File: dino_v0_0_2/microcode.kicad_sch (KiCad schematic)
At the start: 10 parts, among them U15 AT28C64B, U16 74LS244N, U17 74LS244N, U23 AT28C64B, U9 AT28C64B

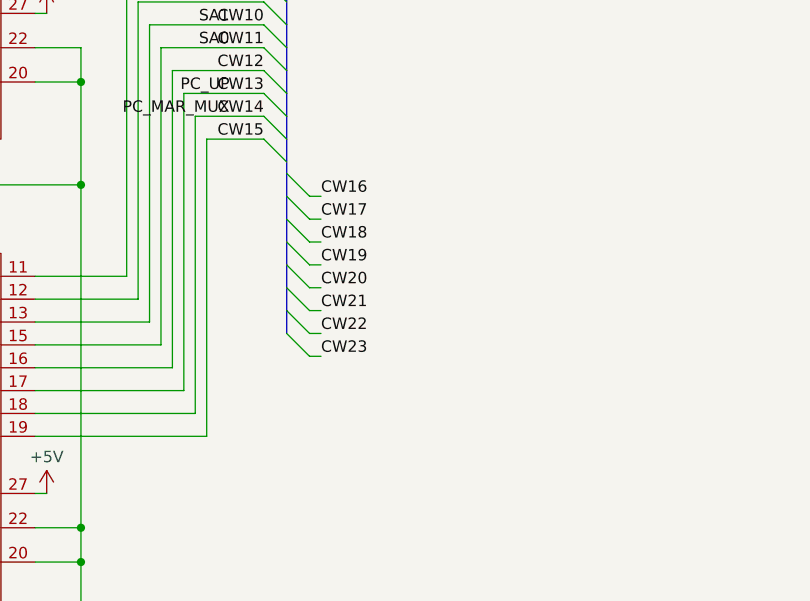
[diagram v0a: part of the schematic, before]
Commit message: feat: Phase F/F+ ISA: 174 instructions, timing fixes, and robust tooling
This commit integrates Phase F and F+ of the ISA, expanding the instruction set to 174 instructions. This includes:
- New conditional branch `JNC`, register-to-register moves, SP/PC readbacks and manipulation (HLSP/SPHL, INXSP/DCXSP).
- Indexed memory access (LDAX/STAX), SP-relative memory access (LDAS/STAS), and memory-indirect addressing (LDAM/STAM/JMPM, etc.) as a new addressing mode.
- Immediate ALU operations (ADI, SUI, ANI, etc.) and ALU results directly to B/C or memory.
- Compare-only instructions (CMP, TST).
- The `IN` opcode has been fully retired from the ISA as of 2026-08-27, and `0x00` confirmed as `NOP`.

Crucially, this commit resolves several critical hardware stability issues:
- Eliminated random machine halts by replacing a damaged `74HC14` (`U56`) and rewiring the reset chain.
- Fixed intermittent failures in `PROG_isasoak` due to ground bounce by starring GND/VCC connections (2026-09-01).
- Introduced microcode-level "SETTLE" states for 23 ALU instructions to ensure timing margins at 1.024MHz, resolving timing-dependent failures for instructions that load and consume operands in consecutive T-states.

The development tooling has also been significantly improved for robustness and accuracy:
- The assembler (`asm.py`) now uses `microcode_gen.py` as the single source of truth for ISA definitions.
- New self-checking ISA tests (`PROG_isa` and variants) were developed, incorporating mutation testing to verify subtest efficacy and provide detailed diagnostic feedback for debugging marginality or hangs.
- The microcode generator enforces hardware constraints at build time (e.g., valid `cond` flag selections, preventing `src=ROM` `dst=RAM` conflicts that led to the `MVI` bug).
- The simulator (`progrom_gen.py`) accurately models `OUT` latching the bus and `dst=RAM` writing to the address bus, and refuses to guess undefined `FLAG_C` states after logic operations.
- The root `Makefile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
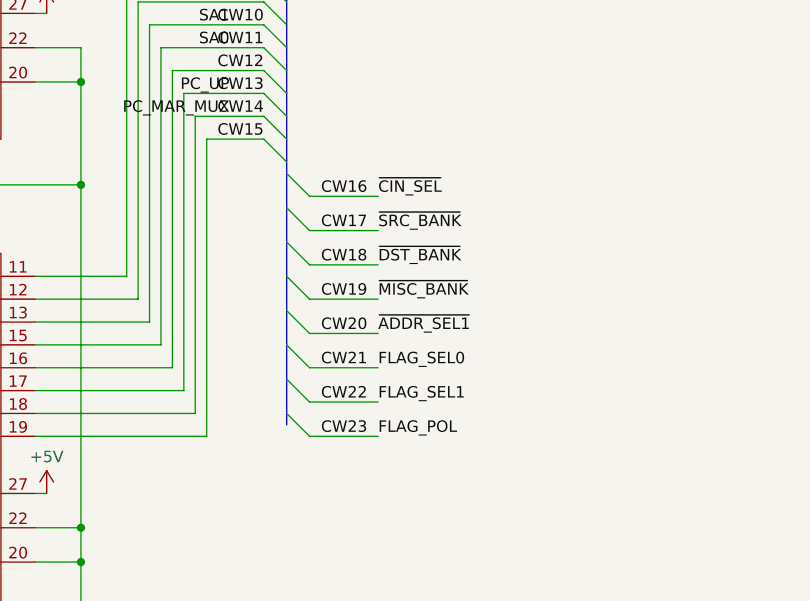
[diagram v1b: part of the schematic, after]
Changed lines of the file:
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@@
 	)
 	(bus_entry
-		(at 171.45 88.9)
-		(size 2.54 2.54)
-		(stroke
-			(width 0)
-			(type default)
-		)
-	)
-	(bus_entry
-		(at 171.45 81.28)
-		(size 2.54 2.54)
-		(stroke
-			(width 0)
-			(type default)
-		)
-	)
-	(bus_entry
-		(at 171.45 91.44)
+		(at 171.45 95.25)
 		(size 2.54 2.54)
 		(stroke
@@
 	)
 	(bus_entry
+		(at 171.45 80.01)
+		(size 2.54 2.54)
+		(stroke
+			(width 0)
+			(type default)
+		)
+	)
+	(bus_entry
 		(at 168.91 34.29)
 		(size 2.54 2.54)
@@
 	)
 	(bus_entry
+		(at 171.45 76.2)
+		(size 2.54 2.54)
+		(stroke
+			(width 0)
+			(type default)
+		)
+	)
+	(bus_entry
 		(at 168.91 64.77)
 		(size 2.54 2.54)
@@
 	)
 	(bus_entry
-		(at 171.45 86.36)
+		(at 168.91 46.99)
 		(size 2.54 2.54)
 		(stroke
@@
 	)
 	(bus_entry
-		(at 171.45 83.82)
+		(at 171.45 91.44)
 		(size 2.54 2.54)
 		(stroke
@@
 	)
 	(bus_entry
-		(at 168.91 46.99)
+		(at 171.45 99.06)
 		(size 2.54 2.54)
 		(stroke
@@
 	)
 	(bus_entry
-		(at 171.45 93.98)
+		(at 171.45 102.87)
 		(size 2.54 2.54)
 		(stroke
@@
 	)
 	(bus_entry
-		(at 171.45 76.2)
+		(at 168.91 57.15)
 		(size 2.54 2.54)
 		(stroke
@@
 	)
 	(bus_entry
-		(at 168.91 57.15)
+		(at 171.45 83.82)
 		(size 2.54 2.54)
 		(stroke
@@
 	)
 	(bus_entry
-		(at 171.45 78.74)
+		(at 171.45 87.63)
 		(size 2.54 2.54)
 		(stroke
@@
 		)
 	)
-	(bus
-		(pts
-			(xy 171.45 88.9) (xy 171.45 91.44)
-		)
-		(stroke
-			(width 0)
-			(type default)
-		)
-	)
 	(wire
 		(pts
@@
 	(wire
 		(pts
-			(xy 173.99 81.28) (xy 175.26 81.28)
+			(xy 173.99 82.55) (xy 181.61 82.55)
 		)
 		(stroke
@@
 	(bus
 		(pts
-			(xy 171.45 86.36) (xy 171.45 88.9)
-		)
-		(stroke
-			(width 0)
-			(type default)
-		)
-	)
-	(bus
-		(pts
 			(xy 171.45 46.99) (xy 171.45 49.53)
 		)
@@
 		)
 	)
-	(bus
-		(pts
-			(xy 171.45 81.28) (xy 171.45 83.82)
-		)
-		(stroke
-			(width 0)
-			(type default)
-		)
-	)
 	(wire
 		(pts
@@
 	(wire
 		(pts
+			(xy 173.99 97.79) (xy 181.61 97.79)
+		)
+		(stroke
+			(width 0)
+			(type default)
+		)
+	)
+	(wire
+		(pts
 			(xy 129.54 190.5) (xy 129.54 194.31)
 		)
@@
 		)
 	)
-	(bus
-		(pts
-			(xy 171.45 76.2) (xy 171.45 78.74)
-		)
-		(stroke
-			(width 0)
-			(type default)
-		)
-	)
 	(wire
 		(pts
@@
 	(wire
 		(pts
-			(xy 173.99 96.52) (xy 175.26 96.52)
+			(xy 173.99 105.41) (xy 181.61 105.41)
 		)
 		(stroke
@@
 	(bus
 		(pts
-			(xy 171.45 78.74) (xy 171.45 81.28)
-		)
-		(stroke
-			(width 0)
-			(type default)
-		)
-	)
-	(bus
-		(pts
 			(xy 26.67 67.31) (xy 29.21 67.31)
 		)
@@
 		)
 	)
-	(bus
-		(pts
-			(xy 171.45 83.82) (xy 171.45 86.36)
-		)
-		(stroke
-			(width 0)
-			(type default)
-		)
-	)
 	(wire
 		(pts
@@
 	(wire
 		(pts
-			(xy 173.99 83.82) (xy 175.26 83.82)
+			(xy 173.99 86.36) (xy 181.61 86.36)
 		)
 		(stroke
@@
 	(wire
 		(pts
-			(xy 173.99 93.98) (xy 175.26 93.98)
+			(xy 173.99 101.6) (xy 181.61 101.6)
 		)
 		(stroke
@@
 	(bus
 		(pts
-			(xy 171.45 74.93) (xy 171.45 76.2)
+			(xy 171.45 74.93) (xy 171.45 104.14)
 		)
 		(stroke
@@
 	(wire
 		(pts
-			(xy 173.99 88.9) (xy 175.26 88.9)
+			(xy 173.99 93.98) (xy 181.61 93.98)
 		)
 		(stroke
@@
 	(wire
 		(pts
-			(xy 173.99 91.44) (xy 175.26 91.44)
-		)
-		(stroke
-			(width 0)
-			(type default)
-		)
-	)
-	(wire
-		(pts
 			(xy 92.71 24.13) (xy 92.71 69.85)
 		)
@@
 	(wire
 		(pts
-			(xy 173.99 78.74) (xy 175.26 78.74)
-		)
-		(stroke
-			(width 0)
-			(type default)
-		)
-	)
-	(bus
-		(pts
-			(xy 171.45 91.44) (xy 171.45 93.98)
+			(xy 173.99 78.74) (xy 181.61 78.74)
 		)
 		(stroke
@@
 	(wire
 		(pts
-			(xy 173.99 86.36) (xy 175.26 86.36)
+			(xy 173.99 90.17) (xy 181.61 90.17)
 		)
 		(stroke
@@
 	)
 	(label "CW22"
-		(at 175.26 93.98 0)
+		(at 175.26 101.6 0)
 		(effects
 			(font
@@
 	)
 	(label "CW18"
-		(at 175.26 83.82 0)
+		(at 175.26 86.36 0)
 		(effects
 			(font
@@
 		)
 	)
+	(label "~{DST_BANK}"
+		(at 181.61 86.36 0)
+		(effects
+			(font
+				(size 1.27 1.27)
+			)
+			(justify left bottom)
+		)
+	)
 	(label "IRB5"
 		(at 31.75 69.85 270)
@@
 	)
 	(label "CW23"
-		(at 175.26 96.52 0)
+		(at 175.26 105.41 0)
 		(effects
 			(font
@@
 	)
 	(label "CW19"
-		(at 175.26 86.36 0)
+		(at 175.26 90.17 0)
 		(effects
 			(font
@@
 	)
 	(label "CW17"
-		(at 175.26 81.28 0)
+		(at 175.26 82.55 0)
 		(effects
 			(font
@@
 		)
 	)
+	(label "~{MISC_BANK}"
+		(at 181.61 90.17 0)
+		(effects
+			(font
+				(size 1.27 1.27)
+			)
+			(justify left bottom)
+		)
+	)
 	(label "IRB1"
 		(at 41.91 69.85 270)
@@
 		)
 	)
+	(label "FLAG_SEL0"
+		(at 181.61 97.79 0)
+		(effects
+			(font
+				(size 1.27 1.27)
+			)
+			(justify left bottom)
+		)
+	)
 	(label "CW5"
 		(at 168.91 46.99 180)
@@
 	)
 	(label "CW21"
-		(at 175.26 91.44 0)
+		(at 175.26 97.79 0)
 		(effects
 			(font
@@
 		)
 	)
+	(label "FLAG_SEL1"
+		(at 181.61 101.6 0)
+		(effects
+			(font
+				(size 1.27 1.27)
+			)
+			(justify left bottom)
+		)
+	)
 	(label "MCA4"
 		(at 113.03 158.75 180)
@@
 		)
 	)
+	(label "FLAG_POL"
+		(at 181.61 105.41 0)
+		(effects
+			(font
+				(size 1.27 1.27)
+			)
+			(justify left bottom)
+		)
+	)
 	(label "~{DST_BANK}"
 		(at 153.67 153.67 0)
@@
 		)
 	)
+	(label "~{SRC_BANK}"
+		(at 181.61 82.55 0)
+		(effects
+			(font
+				(size 1.27 1.27)
+			)
+			(justify left bottom)
+		)
+	)
 	(label "MCA2"
 		(at 86.36 39.37 0)
@@
 	)
 	(label "CW20"
-		(at 175.26 88.9 0)
+		(at 175.26 93.98 0)
 		(effects
 			(font
@@
 		)
 	)
+	(label "~{ADDR_SEL1}"
+		(at 181.61 93.98 0)
+		(effects
+			(font
+				(size 1.27 1.27)
+			)
+			(justify left bottom)
+		)
+	)
+	(label "~{CIN_SEL}"
+		(at 181.61 78.74 0)
+		(effects
+			(font
+				(size 1.27 1.27)
+			)
+			(justify left bottom)
+		)
+	)
